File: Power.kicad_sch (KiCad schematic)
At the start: 21 parts

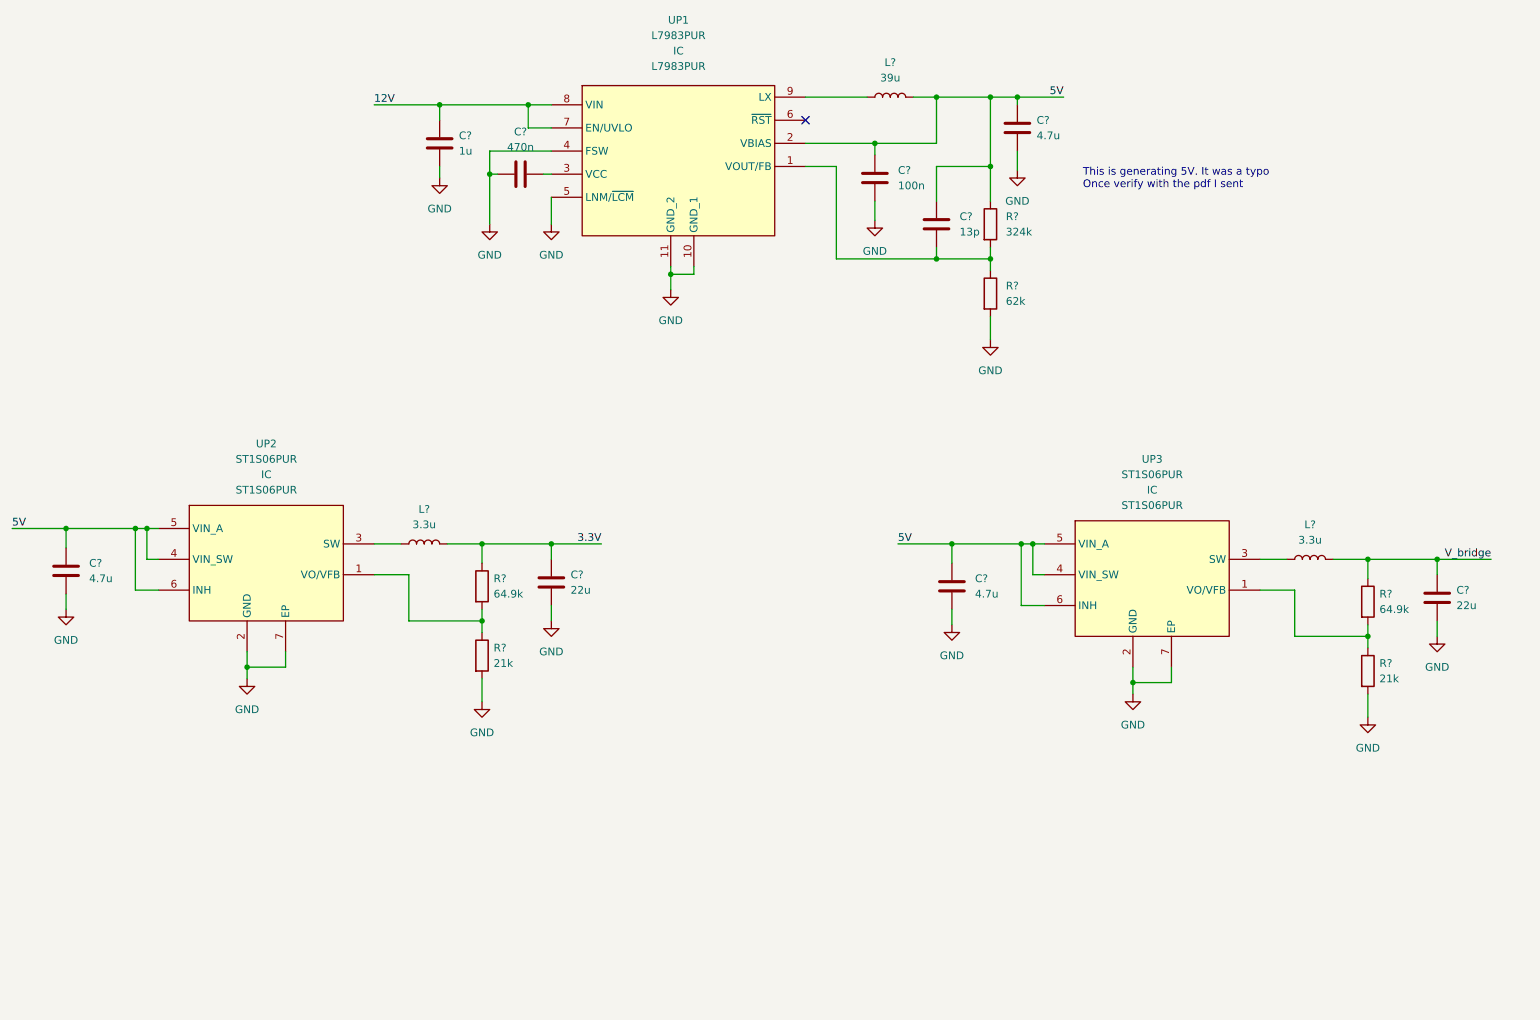
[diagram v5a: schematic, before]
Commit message: eeprom fanned out
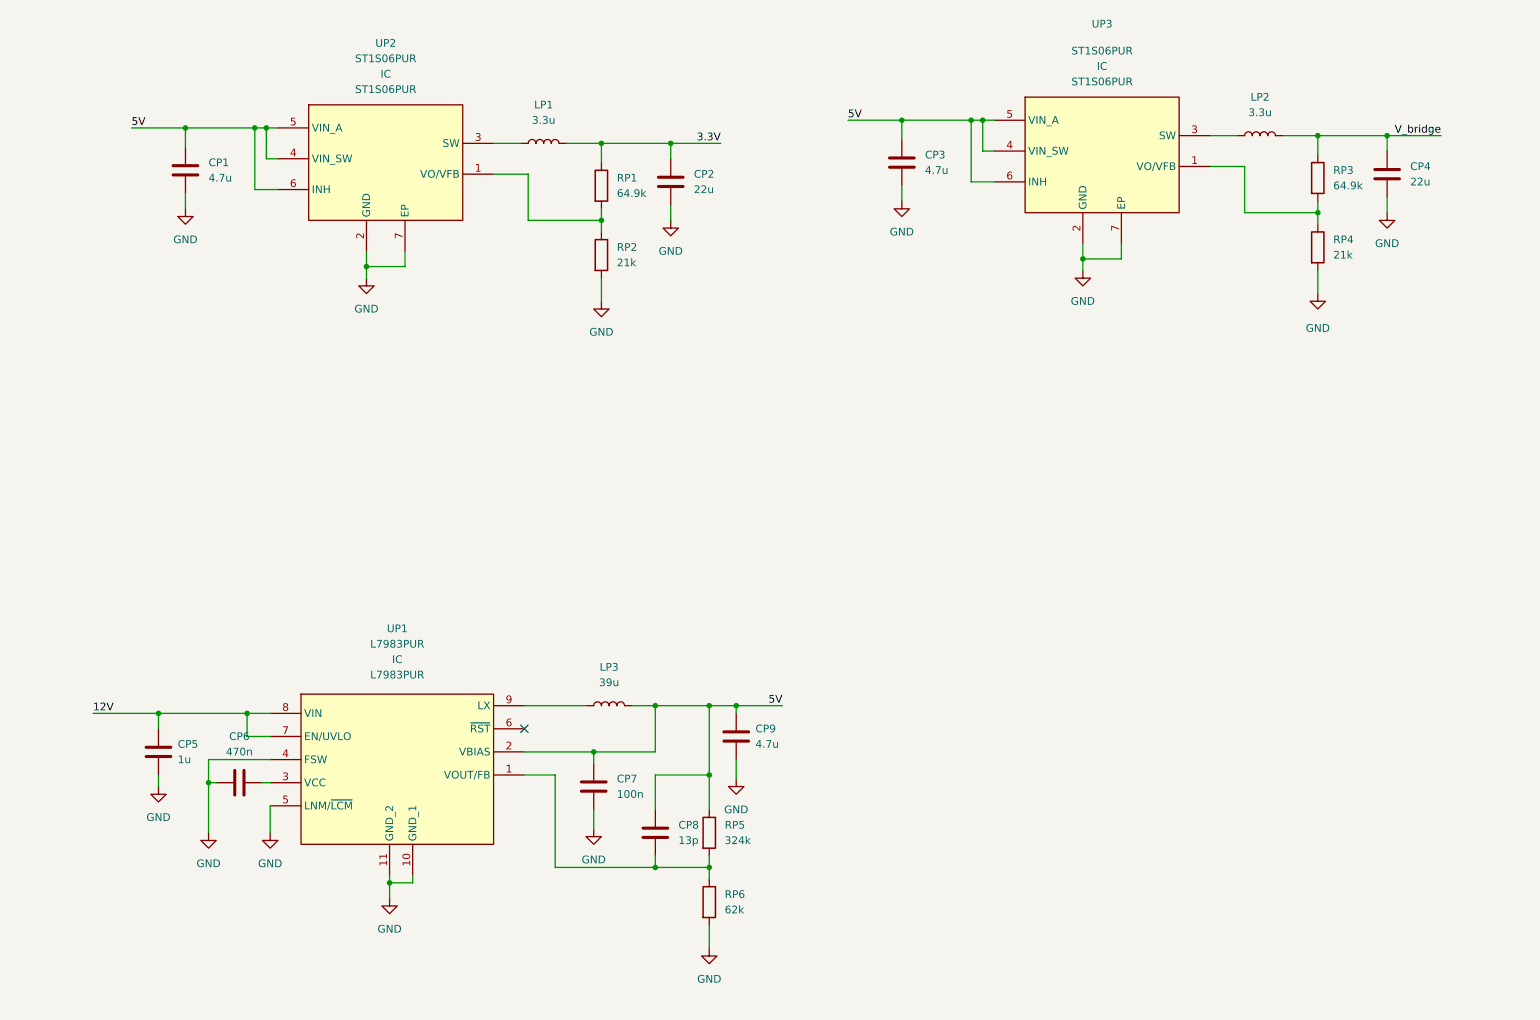
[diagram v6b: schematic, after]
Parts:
- gave numbers to parts that had none: 18
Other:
- note removed: "This is generating 5V. It was a typo Once verify with the pdf I sent"
- moved on the sheet: CP1, CP2, CP3, CP4, CP5, CP6, CP7, CP8, CP9, LP1, LP2, LP3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

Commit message: power supply fanned out
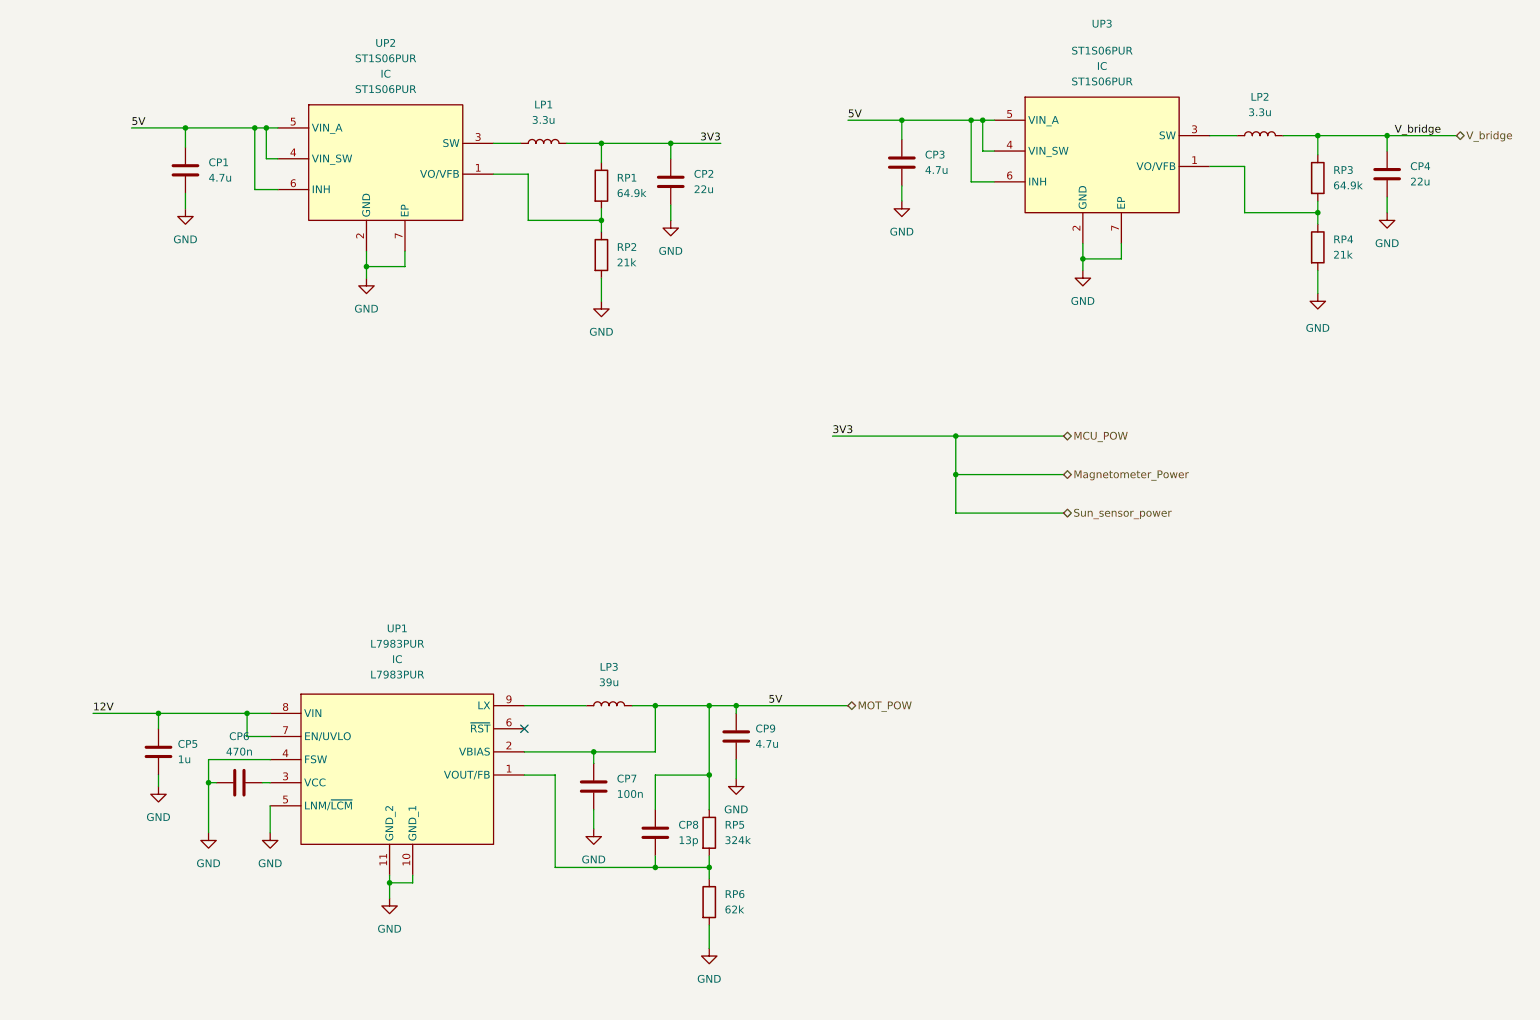
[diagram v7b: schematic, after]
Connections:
- net 3.3V renamed MCU_POW
- net 5V renamed MOT_POW
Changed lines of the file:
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@@
   (junction (at 52.07 33.02) (diameter 0) (color 0 0 0 0)
   )
+  (junction (at 179.07 83.82) (diameter 0) (color 0 0 0 0)
+  )
   (junction (at 129.54 128.27) (diameter 0) (color 0 0 0 0)
   )
@@
   )
   (junction (at 200.025 54.61) (diameter 0) (color 0 0 0 0)
+  )
+  (junction (at 179.07 90.17) (diameter 0) (color 0 0 0 0)
   )
   (junction (at 138.43 128.27) (diameter 0) (color 0 0 0 0)
@@
     (stroke (width 0) (type default) (color 0 0 0 0))
   )
+  (wire (pts (xy 179.07 96.52) (xy 196.85 96.52))
+    (stroke (width 0) (type default) (color 0 0 0 0))
+  )
   (wire (pts (xy 250.19 44.45) (xy 250.19 46.99))
     (stroke (width 0) (type default) (color 0 0 0 0))
@@
     (stroke (width 0) (type default) (color 0 0 0 0))
   )
-  (wire (pts (xy 142.875 128.27) (xy 150.495 128.27))
+  (wire (pts (xy 142.875 128.27) (xy 161.29 128.27))
     (stroke (width 0) (type default) (color 0 0 0 0))
   )
@@
     (stroke (width 0) (type default) (color 0 0 0 0))
   )
+  (wire (pts (xy 179.07 83.82) (xy 196.85 83.82))
+    (stroke (width 0) (type default) (color 0 0 0 0))
+  )
   (wire (pts (xy 129.54 139.7) (xy 138.43 139.7))
     (stroke (width 0) (type default) (color 0 0 0 0))
@@
     (stroke (width 0) (type default) (color 0 0 0 0))
   )
+  (wire (pts (xy 179.07 83.82) (xy 179.07 90.17))
+    (stroke (width 0) (type default) (color 0 0 0 0))
+  )
+  (wire (pts (xy 179.07 90.17) (xy 196.85 90.17))
+    (stroke (width 0) (type default) (color 0 0 0 0))
+  )
   (wire (pts (xy 142.875 137.16) (xy 142.875 140.335))
     (stroke (width 0) (type default) (color 0 0 0 0))
@@
     (stroke (width 0) (type default) (color 0 0 0 0))
   )
-  (wire (pts (xy 250.19 34.29) (xy 259.08 34.29))
+  (wire (pts (xy 250.19 34.29) (xy 261.62 34.29))
     (stroke (width 0) (type default) (color 0 0 0 0))
   )
@@
     (stroke (width 0) (type default) (color 0 0 0 0))
   )
+  (wire (pts (xy 158.75 83.82) (xy 179.07 83.82))
+    (stroke (width 0) (type default) (color 0 0 0 0))
+  )
   (wire (pts (xy 226.695 39.37) (xy 226.695 46.99))
     (stroke (width 0) (type default) (color 0 0 0 0))
@@
   )
   (wire (pts (xy 170.18 42.545) (xy 170.18 45.085))
+    (stroke (width 0) (type default) (color 0 0 0 0))
+  )
+  (wire (pts (xy 179.07 90.17) (xy 179.07 96.52))
     (stroke (width 0) (type default) (color 0 0 0 0))
   )
@@
     (effects (font (size 1.27 1.27)) (justify left bottom))
   )
-  (label "3.3V" (at 140.335 35.56 180)
+  (label "3V3" (at 158.75 83.82 0)
+    (effects (font (size 1.27 1.27)) (justify left bottom))
+  )
+  (label "3V3" (at 140.335 35.56 180)
     (effects (font (size 1.27 1.27)) (justify right bottom))
   )
@@
     (effects (font (size 1.27 1.27)) (justify left bottom))
   )
+  (hierarchical_label "MCU_POW" (shape bidirectional) (at 196.85 83.82 0)
+    (effects (font (size 1.27 1.27)) (justify left))
+  )
+  (hierarchical_label "Sun_sensor_power" (shape bidirectional) (at 196.85 96.52 0)
+    (effects (font (size 1.27 1.27)) (justify left))
+  )
+  (hierarchical_label "MOT_POW" (shape bidirectional) (at 161.29 128.27 0)
+    (effects (font (size 1.27 1.27)) (justify left))
+  )
+  (hierarchical_label "V_bridge" (shape bidirectional) (at 261.62 34.29 0)
+    (effects (font (size 1.27 1.27)) (justify left))
+  )
+  (hierarchical_label "Magnetometer_Power" (shape bidirectional) (at 196.85 90.17 0)
+    (effects (font (size 1.27 1.27)) (justify left))
+  )
   (symbol (lib_id "power:GND") (at 52.07 46.355 0) (unit 1)

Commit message: Interboard added
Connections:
- net MOT_POW renamed 5V
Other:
- note added: "Put up a text box showing calculation for output voltage for each reg"
- note added: "We need Motor power to be above 5 V say 5.2 or 5.5"
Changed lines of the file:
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@@
     (stroke (width 0) (type default) (color 0 0 0 0))
+  )
+  (text "Put up a text box \nshowing calculation for \noutput voltage for each reg "
+    (at 90.17 91.44 0)
+    (effects (font (size 1.778 1.778)) (justify left bottom))
+  )
+  (text "We need Motor power to\nbe above 5 V say 5.2 or 5.5 \n"
+    (at 64.77 177.8 0)
+    (effects (font (size 1.27 1.27)) (justify left bottom))
   )
   (label "5V" (at 150.495 128.27 180)
@@
     (effects (font (size 1.27 1.27)) (justify left))
   )
+  (hierarchical_label "12V" (shape bidirectional) (at 36.83 129.54 180)
+    (effects (font (size 1.27 1.27)) (justify right))
+  )
+  (hierarchical_label "5V" (shape bidirectional) (at 161.29 31.75 180)
+    (effects (font (size 1.27 1.27)) (justify right))
+  )
   (hierarchical_label "Sun_sensor_power" (shape bidirectional) (at 196.85 96.52 0)
     (effects (font (size 1.27 1.27)) (justify left))
   )
+  (hierarchical_label "5V" (shape bidirectional) (at 43.18 33.02 180)
+    (effects (font (size 1.27 1.27)) (justify right))
+  )
   (hierarchical_label "MOT_POW" (shape bidirectional) (at 161.29 128.27 0)
